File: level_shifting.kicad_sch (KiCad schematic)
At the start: 22 parts, among them J49 Conn_01x08, J50 Conn_01x04, J51 Conn_01x08, U25 TXS0108EPW

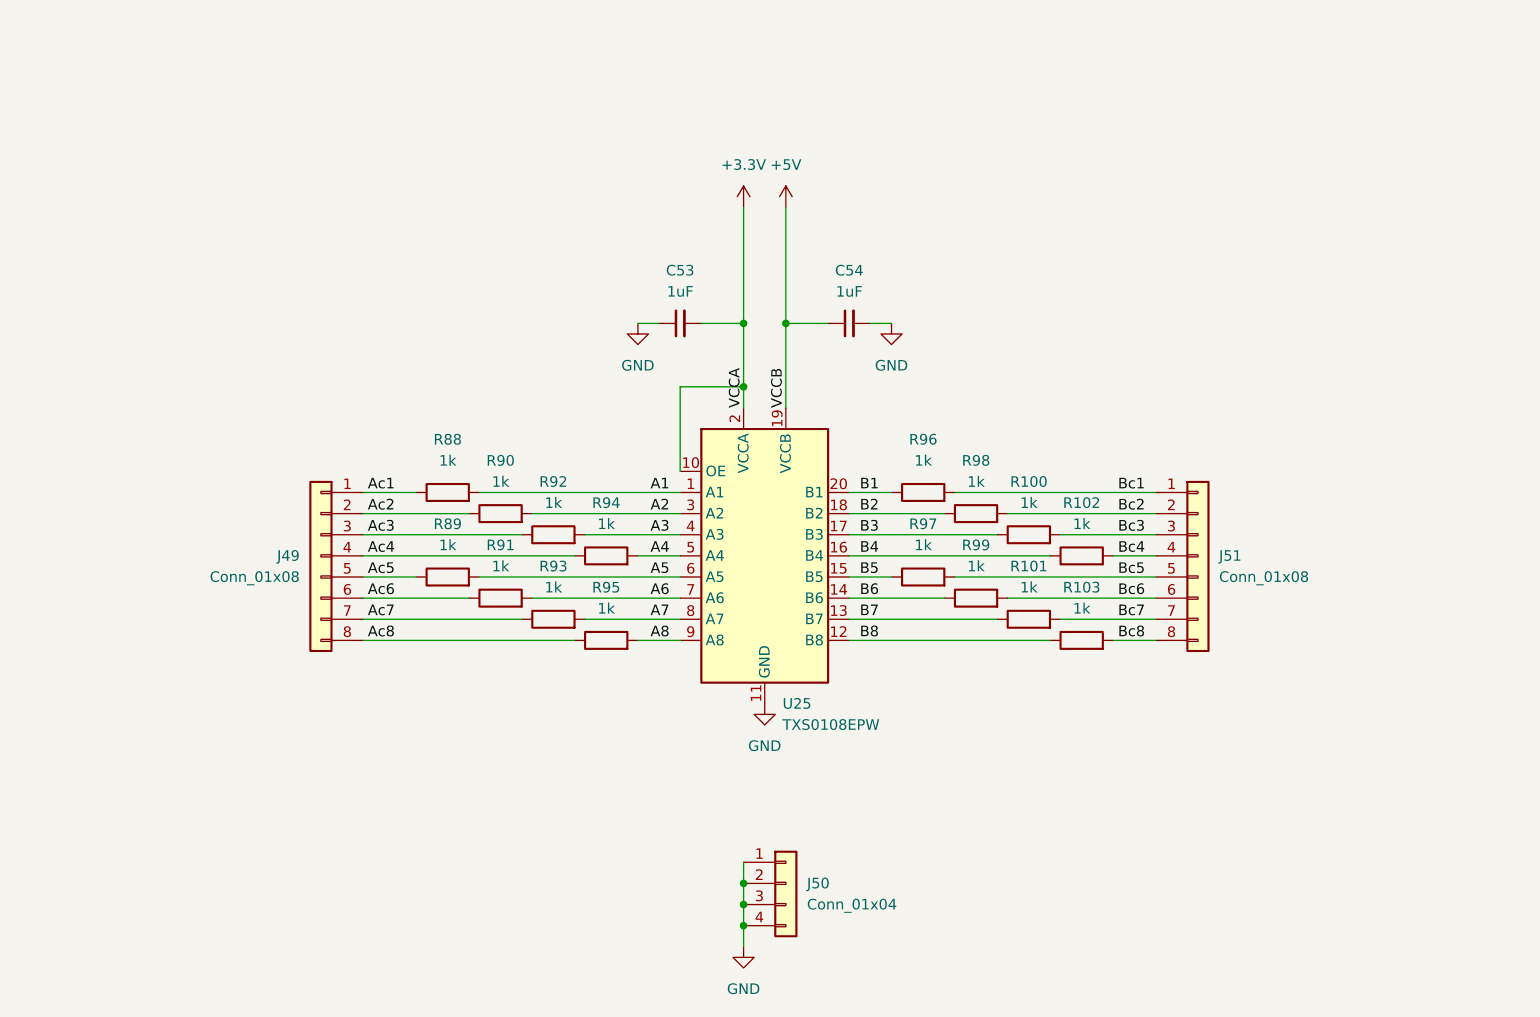
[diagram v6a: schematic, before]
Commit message: Update the design to a stackable one
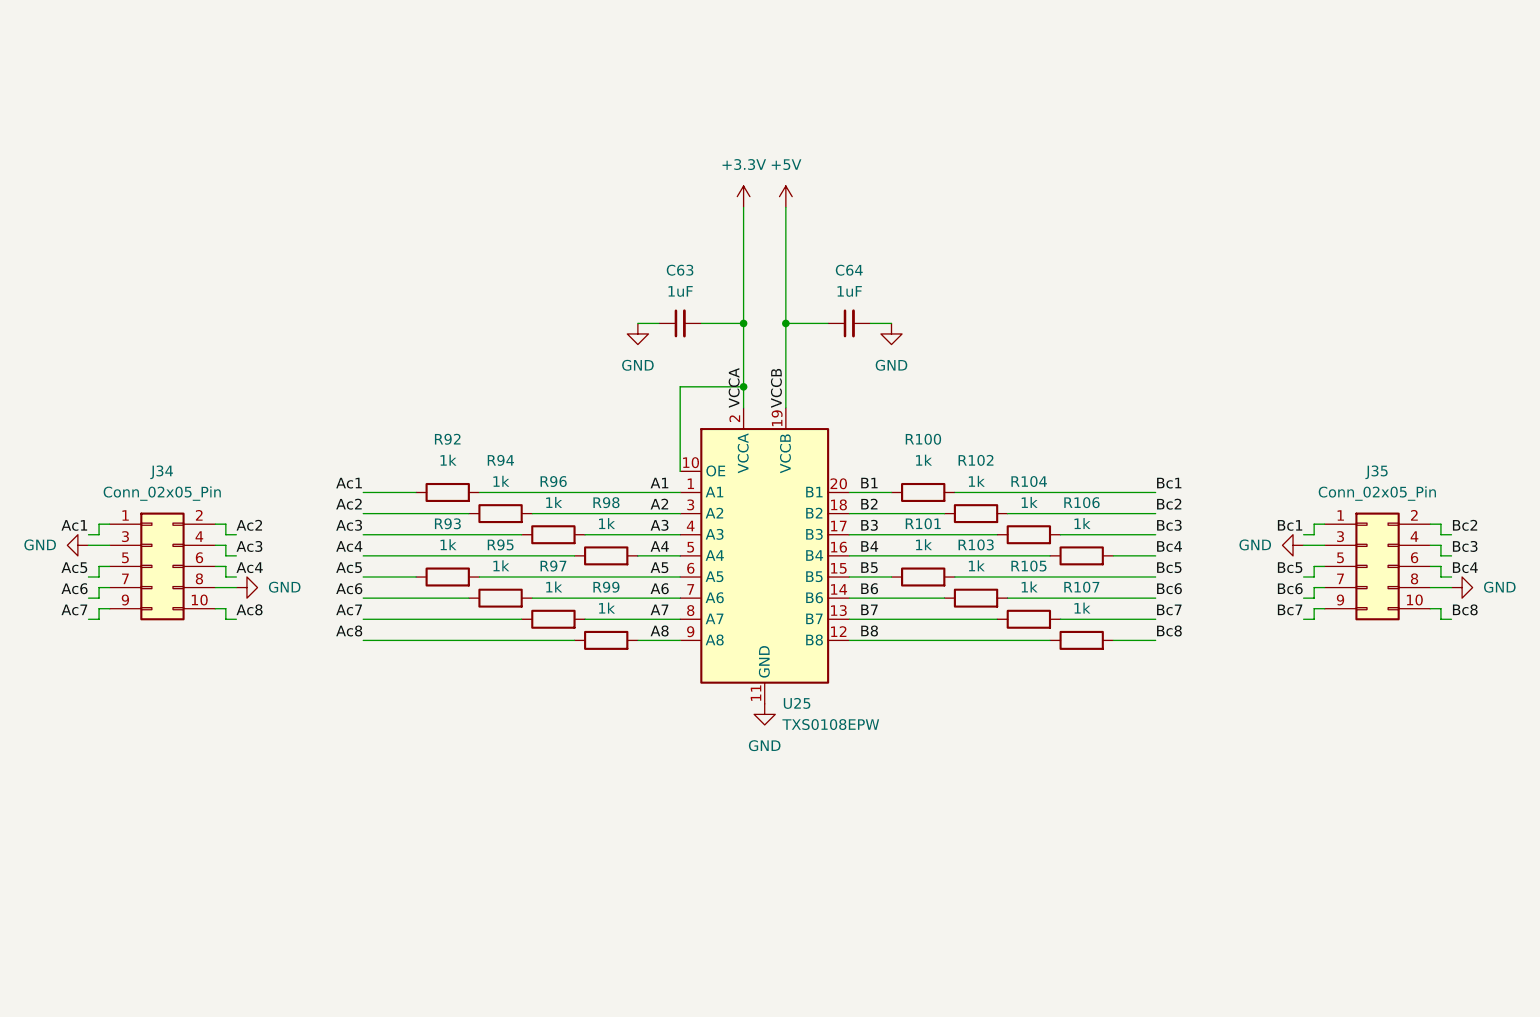
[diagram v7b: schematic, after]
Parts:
- removed J50: Conn_01x04, HL_Connector_Pad_2.54mm:Pad_1x04_P2.54_1.7x1.7_Rect, symbol Connector_Generic:Conn_01x04
- J34: renamed from J49; value Conn_01x08 -> Conn_02x05_Pin; footprint HL_Connector_Pad_2.54mm:Pad_1x08_P2.54_1.7x1.7_Oct -> HL_Connector_Pad_2.54mm:Pad_2x05_P2.54_1.7x1.7_2Rect-8Oct; symbol Connector_Generic:Conn_01x08 -> Connector_Generic:Conn_02x05_Odd_Even; JLCPCB_CORRECTION 0;8.89;270 -> 1.27;-5.08;270; LCSC C492407 -> C492422
- J35: renamed from J51; value Conn_01x08 -> Conn_02x05_Pin; footprint HL_Connector_Pad_2.54mm:Pad_1x08_P2.54_1.7x1.7_Oct -> HL_Connector_Pad_2.54mm:Pad_2x05_P2.54_1.7x1.7_2Rect-8Oct; symbol Connector_Generic:Conn_01x08 -> Connector_Generic:Conn_02x05_Odd_Even; JLCPCB_CORRECTION 0;8.89;270 -> 1.27;-5.08;270; LCSC C492407 -> C492422
- renumbered C53 to C63, C54 to C64, R96 to R100, R97 to R101, R98 to R102, R99 to R103, R100 to R104, R101 to R105, R102 to R106, R103 to R107, R88 to R92, R89 to R93, R90 to R94, R91 to R95, R92 to R96, R93 to R97, R94 to R98, R95 to R99
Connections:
- net Ac3: now also J34.4 (Pin_4); no longer J34.3 (Pin_3)
- net Ac4: now also J34.6 (Pin_6); no longer J34.4 (Pin_4)
- net Ac6: now also J34.7 (Pin_7); no longer J34.6 (Pin_6)
- net Ac7: now also J34.9 (Pin_9); no longer J34.7 (Pin_7)
- net Ac8: now also J34.10 (Pin_10); no longer J34.8 (Pin_8)
- net Bc3: now also J35.4 (Pin_4); no longer J35.3 (Pin_3)
- net Bc4: now also J35.6 (Pin_6); no longer J35.4 (Pin_4)
- net Bc6: now also J35.7 (Pin_7); no longer J35.6 (Pin_6)
- net Bc7: now also J35.9 (Pin_9); no longer J35.7 (Pin_7)
- net Bc8: now also J35.10 (Pin_10); no longer J35.8 (Pin_8)
- net GND: now also J34.3 (Pin_3), J34.8 (Pin_8), J35.3 (Pin_3), J35.8 (Pin_8)
